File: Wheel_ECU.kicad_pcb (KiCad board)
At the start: 2 copper layers, 61 x 61 mm, 59 parts, among them J1 Conn_01x04, J2 Conn_01x04, J3 Conn_01x02, J4 Debug, U1 BD6211F, U2 TLE4964, U3 XMC1404_F064, U4 TLE7251

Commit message: Add Wolley Interconnect logo footprint to local library
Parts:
- G***: footprint DammR8:Wolley_Interconnect_Logotype -> WheelECU:Logo_Wolley_Interconnect_SolderMask

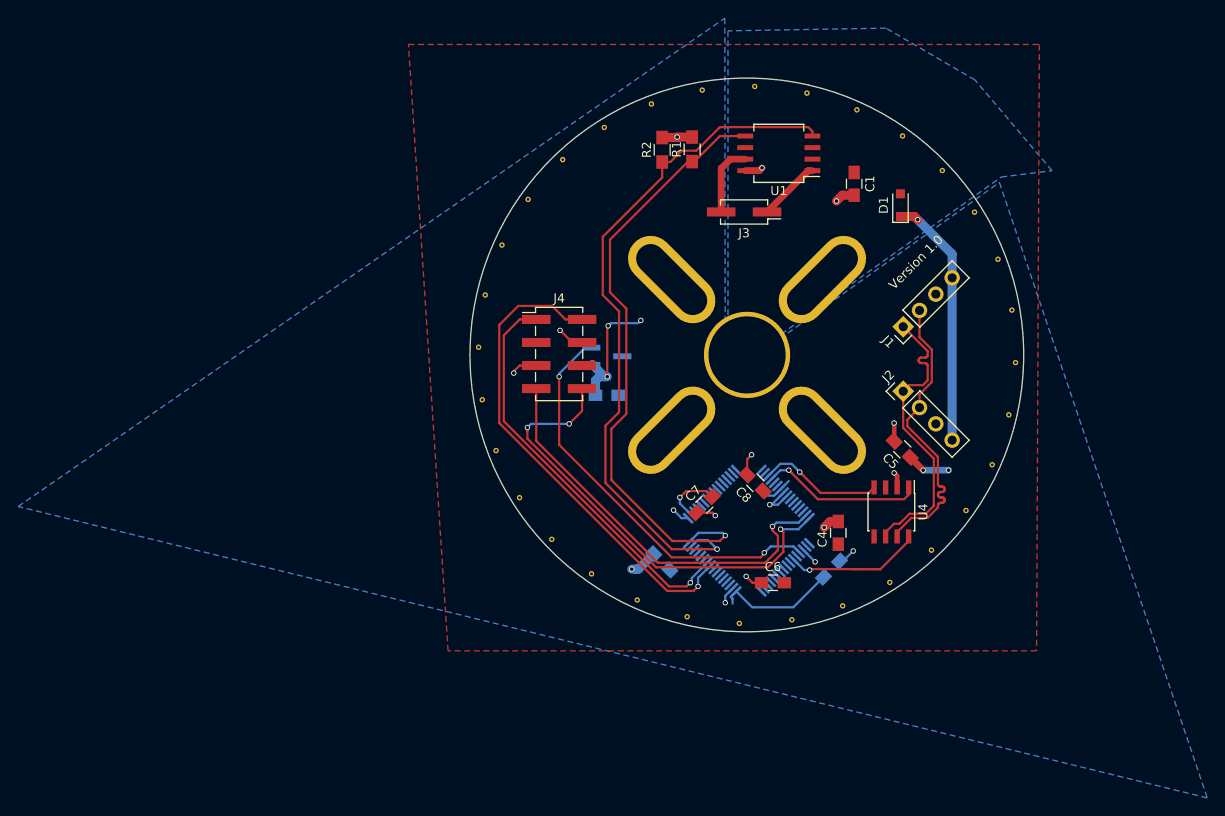
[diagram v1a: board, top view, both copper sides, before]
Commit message: Replace the motor driver and other improvements
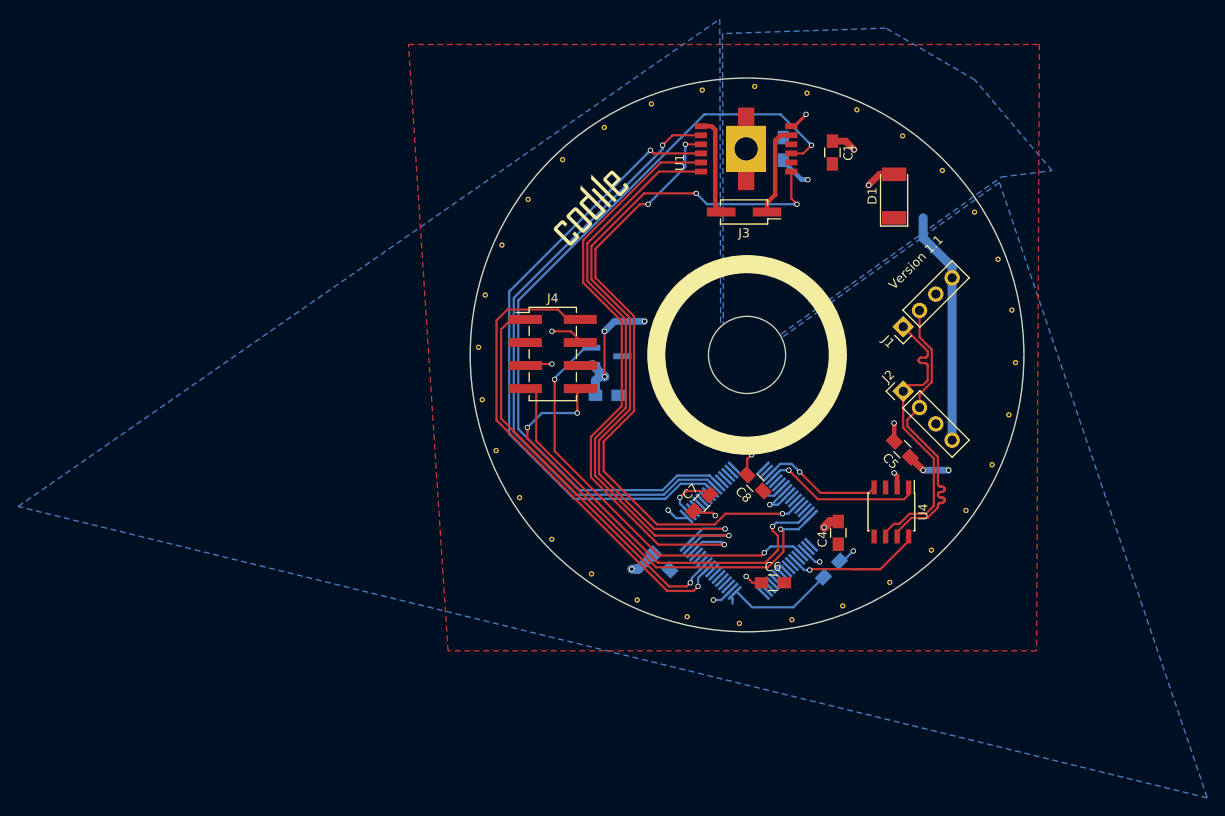
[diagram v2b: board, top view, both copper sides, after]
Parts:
- removed the G*** at (114.5, 81.7)
- removed R1, R2: 10K, Resistors_SMD:R_0805_HandSoldering
- added C10: 100uF, Capacitors_SMD:C_0805_HandSoldering, B.Cu at (135.8, 75.7)
- added G***: LOGO, WheelECU:Logo_Codile_SilkScreen_4mm, F.Cu at (114.2, 81.8)
- C1: value 10uF -> 1uF
- D1: value TVS_Diode -> SMF5.0A; footprint Diodes_SMD:D_SOD-323_HandSoldering -> Diodes_SMD:D_MELF
- J4: footprint Pin_Headers:Pin_Header_Straight_2x04_Pitch2.54mm_SMD -> WheelECU:Pin_Header_Straight_2x04_Pitch2.54mm_SMD
- M** (x4): footprint Mount_Holes:Mount_Hole_M3x6.5 -> WheelECU:Mount_Hole_M3x6.5
- M**: footprint Mount_Holes:Motor_Center_Hole -> WheelECU:Motor_Center_Hole
- U1: value BD6211F -> IFX9201SG; footprint Housings_SOIC:SO-8_5.3x6.2mm_Pitch1.27mm -> WheelECU:SOIC-12_HeatSlugs
- U3: footprint Housings_QFP:TQFP-64_10x10mm_Pitch0.5mm -> WheelECU:TQFP-64_10x10mm_Pitch0.5mm_Handsoldering
- moved C1 4.20 mm to (141.2, 76.1)
- moved U1 3.63 mm to (131.7, 75.7), turned to 90 degrees
- moved D1 1.22 mm to (148.0, 80.9)
- moved J4 0.70 mm to (110.4, 98.3)
- moved C7 0.36 mm to (126.8, 114.7)
- turned M** to 45 degrees
- turned M** to 135 degrees (x2)
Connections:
- net Net-(J3-Pad2) renamed MOTOR_OUT2
- C1 pad 1: +5V -> GND
- C1 pad 2: GND -> +5V
- D1 pad 1: GND -> +5V
- D1 pad 2: +5V -> GND
- J3 pad 1: Net-(J3-Pad1) -> MOTOR_OUT1
- U1 pad 1: Net-(J3-Pad1) -> MOTOR_DIRECTION
- U1 pad 3: +5V -> MISO
- U1 pad 4: MOTOR_FORWARD -> +5V
- U1 pad 5: MOTOR_REVERSE -> MOTOR_OUT1
- U1 pad 6: +5V -> GND
- U1 pad 8: GND -> MOSI
- U3 pad 10: Net-(U3-Pad10) -> MOSI
- U3 pad 11: Net-(U3-Pad11) -> MISO
- U3 pad 28: Net-(U3-Pad28) -> MOTOR_DRIVER_SS
- U3 pad 62: Net-(U3-Pad62) -> MOTOR_DISABLE
- U3 pad 63: MOTOR_FORWARD -> MOTOR_PWM
- U3 pad 64: MOTOR_REVERSE -> MOTOR_DIRECTION
- U3 pad 9: Net-(U3-Pad9) -> SCLK
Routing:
- net MISO: track 0.00 -> 85.0 mm, vias 0 -> 1
- net MOTOR_DIRECTION: track 0.00 -> 78.8 mm, vias 0 -> 3
- net MOTOR_FORWARD: track 77.2 -> 0.00 mm, vias 1 -> 0
- net MOTOR_DRIVER_SS: track 0.00 -> 70.3 mm, vias 0 -> 3
- net SCLK: track 0.00 -> 69.7 mm, vias 0 -> 1
- net MOSI: track 0.00 -> 69.2 mm, vias 0 -> 1
- net MOTOR_REVERSE: track 67.8 -> 0.00 mm, vias 1 -> 0
- net MOTOR_DISABLE: track 0.00 -> 67.6 mm, vias 0 -> 1
- net MOTOR_PWM: track 0.00 -> 66.7 mm, vias 0 -> 1
- net MOTOR_OUT1: track 0.00 -> 10.2 mm
- net Net-(J3-Pad1): track 6.88 -> 0.00 mm
- net GND: track 71.9 -> 77.9 mm, vias 13 -> 12
- net +5V: track 39.4 -> 44.8 mm, vias 11 -> 12
- net MOTOR_OUT2: track 7.87 -> 11.1 mm
- net SPEED_SENSOR_OUTPUT: track 45.1 -> 45.9 mm
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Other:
- board text added: "Version 1.1"
- board text removed: "Version 1.0"

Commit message: Copy the changes from the CentrifugalFan module
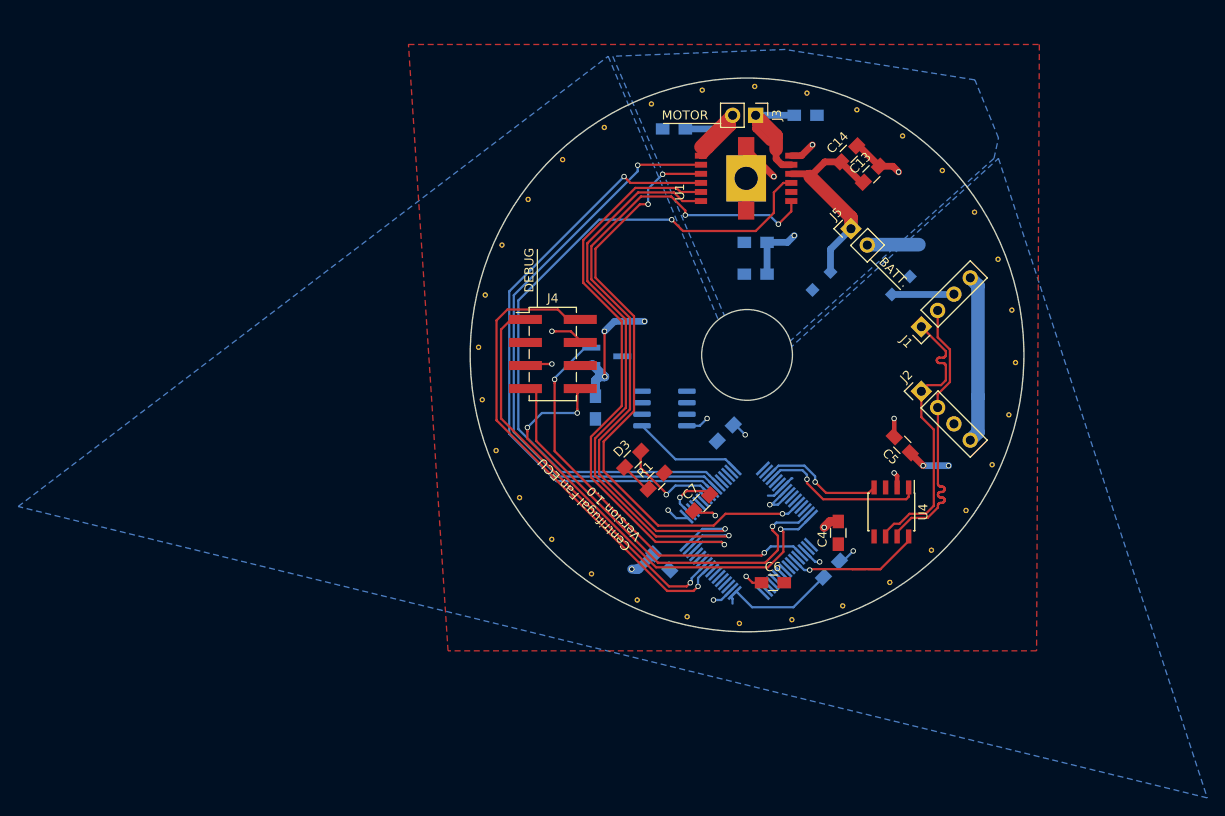
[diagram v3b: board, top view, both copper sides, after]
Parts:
- removed the G*** at (114.2, 81.8)
- removed the M** at (140.1, 90.1)
- removed the M** at (123.5, 106.7)
- added C11: 30nF, WheelECU:C_0805_HandSoldering, B.Cu at (123.8, 73.5)
- added C12: 30nF, WheelECU:C_0805_HandSoldering, B.Cu at (138.2, 72.0)
- added C13: 100uF, WheelECU:C_0805_HandSoldering, F.Cu at (145.5, 78.5)
- added C14: 100nF, WheelECU:C_0805_HandSoldering, F.Cu at (143.0, 76.2)
- added D2: SMF36A, Diode_SMD:D_SOD-123F, B.Cu at (140.0, 90.2)
- added D3: LED, WheelECU:C_0805_HandSoldering, F.Cu at (119.2, 109.9)
- added J5: Conn_01x02, Connector_PinHeader_2.54mm:PinHeader_1x02_P2.54mm_Vertical, F.Cu at (143.2, 84.5)
- added R1: R, WheelECU:C_0805_HandSoldering, F.Cu at (121.8, 112.3)
- added U5: LM35-D, Package_SO:SOIC-8_3.9x4.9mm_P1.27mm, B.Cu at (122.7, 104.3)
- C1, C8: moved to B.Cu
- D1: footprint Diodes_SMD:D_MELF -> Diode_SMD:D_SOD-123F; moved to B.Cu
- J3: footprint Pin_Headers:Pin_Header_Straight_2x01_Pitch2.54mm_SMD -> Connector_PinHeader_2.54mm:PinHeader_1x02_P2.54mm_Vertical
- moved G*** 46.4 mm to (113.0, 81.3)
- moved C10 14.1 mm to (132.8, 89.5), turned to 0 degrees
- moved C1 13.0 mm to (132.8, 86.0), turned to 0 degrees
- moved J3 10.7 mm to (132.8, 72.0), turned to 270 degrees
- moved D1 9.88 mm to (148.8, 90.8), turned to 45 degrees
- moved C8 6.41 mm to (129.4, 107.0), turned to 45 degrees
- moved U1 3.25 mm to (131.7, 79.0)
- moved J1 2.00 mm to (151.0, 95.3)
- moved J2 2.00 mm to (151.0, 102.4)
- moved C2 1.84 mm to (115.1, 104.2), turned to 90 degrees
- moved C5 0.50 mm to (148.9, 108.3)
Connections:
- U1 pad 4: +5V -> +BATT
- U3 pad 16: Net-(U3-Pad16) -> TEMP_SENSOR_OUTPUT
- U3 pad 8: Net-(U3-Pad8) -> STATUS_LED
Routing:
- net +BATT: track 0.00 -> 23.0 mm
- net +5V: track 44.8 -> 59.1 mm, vias 12 -> 14
- net TEMP_SENSOR_OUTPUT: track 0.00 -> 12.2 mm
- net STATUS_LED: track 0.00 -> 11.5 mm, vias 0 -> 1
- net MISO: track 85.0 -> 76.6 mm
- net MOTOR_OUT2: track 11.1 -> 19.1 mm
- net MOTOR_OUT1: track 10.2 -> 15.6 mm
- net Net-(D3-Pad2): track 0.00 -> 3.59 mm
- net GND: track 77.9 -> 80.5 mm, vias 12 -> 11
- net SCLK: track 69.7 -> 67.3 mm
- net MOSI: track 69.2 -> 66.8 mm
- net CAN+: track 32.8 -> 30.9 mm
- net MOTOR_DRIVER_SS: track 70.3 -> 68.6 mm
- net MOTOR_DIRECTION: track 78.8 -> 77.1 mm
- net MOTOR_DISABLE: track 67.6 -> 66.6 mm
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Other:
- board text added: "BATT."
- board text added: "Centrifugal Fan ECU Version 1.0"
- board text added: "DEBUG"
- board text added: "MOTOR"
- board text removed: "Version 1.1"

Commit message: Change the version text on the PCB
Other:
- board text added: "Version 1.2"
- board text removed: "Centrifugal Fan ECU Version 1.0"

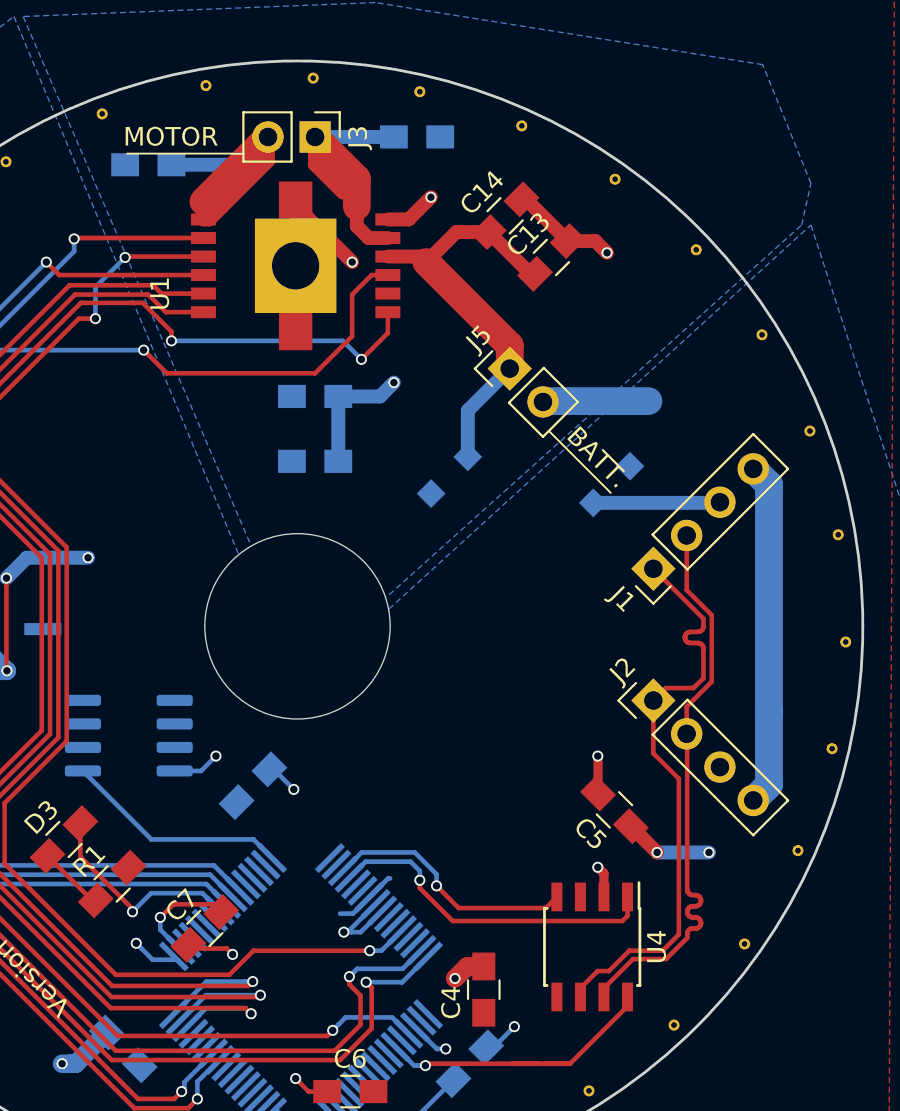
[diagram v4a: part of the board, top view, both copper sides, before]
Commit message: Move connectors closer to middle
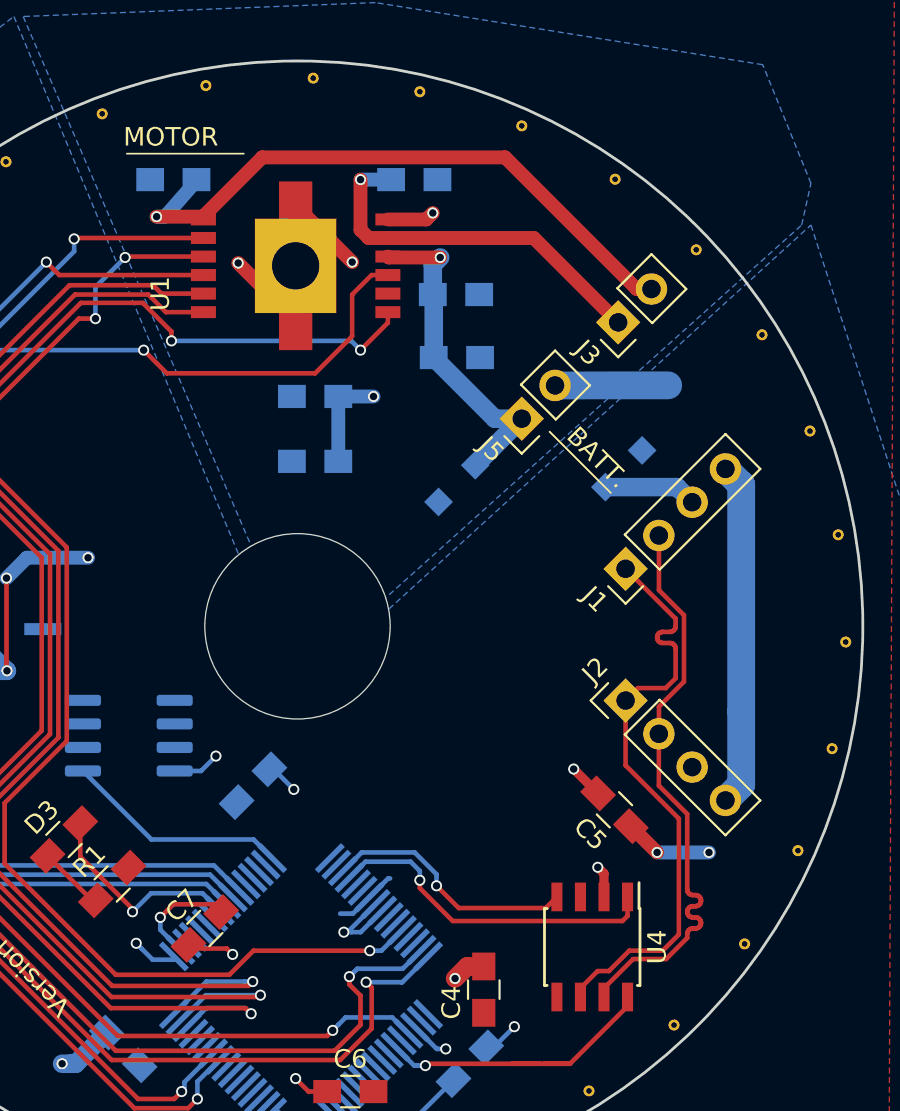
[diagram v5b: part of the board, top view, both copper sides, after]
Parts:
- C13, C14: moved to B.Cu
- moved J3 19.2 mm to (149.1, 82.0), turned to 135 degrees
- moved C14 8.08 mm to (140.4, 83.9), turned to 0 degrees
- moved C13 5.52 mm to (140.3, 80.5), turned to 0 degrees
- moved J5 2.78 mm to (143.9, 87.2), turned to 135 degrees
- moved C12 2.30 mm to (138.1, 74.3)
- moved C11 1.57 mm to (125.1, 74.3)
- moved J1 1.50 mm to (149.5, 95.3)
- moved J2 1.50 mm to (149.5, 102.4)
- moved D1 1.07 mm to (149.4, 89.9)
- moved D2 0.60 mm to (140.4, 90.7)
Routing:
- net MOTOR_OUT2: track 19.1 -> 33.9 mm, vias 0 -> 1
- net +BATT: track 23.0 -> 18.1 mm, vias 0 -> 1
- net MOTOR_OUT1: track 15.6 -> 20.3 mm, vias 0 -> 1
- net +5V: track 59.1 -> 55.9 mm
- net MOTOR_DIRECTION: track 77.1 -> 76.4 mm
- net CAN-: track 31.9 -> 32.5 mm
- net CAN+: track 30.9 -> 31.5 mm

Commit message: Smaller clean up
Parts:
- moved G*** 0.23 mm to (113.1, 81.5)
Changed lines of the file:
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@@
   )
   (setup
-    (last_trace_width 1)
+    (last_trace_width 0.75)
     (user_trace_width 0.35)
     (user_trace_width 0.5)
@@
   )
   (module WheelECU:Logo_Wolley_Interconnect_SolderMask (layer F.Cu)
-    (at 113.03 81.28)
+    (at 113.1 81.5)
     (fp_text reference G*** (at 0 0) (layer F.SilkS) hide
       (effects (font (size 1.524 1.524) (thickness 0.3)))
@@
   (segment (start 135.666116 113.02642) (end 136.692536 112) (width 0.25) (layer B.Cu) (net 1))
   (segment (start 136.692536 112) (end 136.8 112) (width 0.25) (layer B.Cu) (net 1))
-  (segment (start 148.016117 107.416117) (end 146.7 106.1) (width 0.5) (layer F.Cu) (net 1))
   (via (at 146.7 106.1) (size 0.6) (drill 0.4) (layers F.Cu B.Cu) (net 1))
   (segment (start 151.8 85.4) (end 145.696051 85.403949) (width 1.5) (layer B.Cu) (net 1))
@@
   (segment (start 131.7 81.9) (end 128.6 78.8) (width 0.75) (layer F.Cu) (net 1))
   (segment (start 131.7 82.5) (end 131.7 81.9) (width 0.75) (layer F.Cu) (net 1))
+  (segment (start 148.016117 107.416117) (end 146.7 106.1) (width 0.75) (layer F.Cu) (net 1))
   (segment (start 151.2 110.6) (end 154 110.6) (width 0.75) (layer B.Cu) (net 2))
   (via (at 154 110.6) (size 0.6) (drill 0.4) (layers F.Cu B.Cu) (net 2))

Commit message: Add key hole
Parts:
- removed the REF** at (161.4, 99.2)
- added REF**: Key_Hole_3mm, WheelECU:Key_Hole_3mm, F.Cu at (162.3, 98.4)
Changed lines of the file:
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@@
     (add_net CAN-)
+  )
+  (module WheelECU:Key_Hole_3mm (layer F.Cu)
+    (at 162.3 98.4)
+    (fp_text reference REF** (at 0 2.54) (layer F.SilkS) hide
+      (effects (font (size 1 1) (thickness 0.15)))
+    )
+    (fp_text value Key_Hole_3mm (at 0 -2.54) (layer F.Fab)
+      (effects (font (size 1 1) (thickness 0.15)))
+    )
+    (pad "" np_thru_hole circle (at 0 0) (size 3 3) (drill 3) (layers *.Cu *.Mask))
   )
   (module WheelECU:Motor_Center_Hole (layer F.Cu)
@@
     )
     (pad 1 thru_hole circle (at 0 0 33.75) (size 0.6 0.6) (drill 0.3) (layers *.Cu)
-      (net 1 GND) (zone_connect 2))
-  )
-  (module Mount_Holes:Edge_Via (layer F.Cu)
-    (at 161.375217 99.24649 22.5)
-    (fp_text reference REF** (at 0.1 1.6 22.5) (layer F.SilkS) hide
-      (effects (font (size 1 1) (thickness 0.15)))
-    )
-    (fp_text value Edge_Via (at -0.1 -1.8 22.5) (layer F.Fab) hide
-      (effects (font (size 1 1) (thickness 0.15)))
-    )
-    (pad 1 thru_hole circle (at 0 0 22.5) (size 0.6 0.6) (drill 0.3) (layers *.Cu)
       (net 1 GND) (zone_connect 2))
   )
@@
   (gr_circle (center 131.8 98.4) (end 162.3 98.5) (layer Edge.Cuts) (width 0.15))
   (dimension 61 (width 0.3) (layer Dwgs.User)
-    (gr_text 61,000mm (at 131.8 58.55) (layer Dwgs.User)
+    (gr_text 61,000mm (at 131.8 58.05) (layer Dwgs.User)
       (effects (font (size 1.5 1.5) (thickness 0.3)))
     )
-    (feature1 (pts (xy 162.3 99) (xy 162.3 57.2)))
-    (feature2 (pts (xy 101.3 99) (xy 101.3 57.2)))
-    (crossbar (pts (xy 101.3 59.9) (xy 162.3 59.9)))
-    (arrow1a (pts (xy 162.3 59.9) (xy 161.173496 60.486421)))
-    (arrow1b (pts (xy 162.3 59.9) (xy 161.173496 59.313579)))
-    (arrow2a (pts (xy 101.3 59.9) (xy 102.426504 60.486421)))
-    (arrow2b (pts (xy 101.3 59.9) (xy 102.426504 59.313579)))
+    (feature1 (pts (xy 162.3 98.5) (xy 162.3 56.7)))
+    (feature2 (pts (xy 101.3 98.5) (xy 101.3 56.7)))
+    (crossbar (pts (xy 101.3 59.4) (xy 162.3 59.4)))
+    (arrow1a (pts (xy 162.3 59.4) (xy 161.173496 59.986421)))
+    (arrow1b (pts (xy 162.3 59.4) (xy 161.173496 58.813579)))
+    (arrow2a (pts (xy 101.3 59.4) (xy 102.426504 59.986421)))
+    (arrow2b (pts (xy 101.3 59.4) (xy 102.426504 58.813579)))
   )
   (gr_text "Version 1.2" (at 119.3 119.2 135) (layer F.SilkS)
